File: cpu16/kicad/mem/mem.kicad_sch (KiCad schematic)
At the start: 16 parts, among them J2 BACKPLANE_2x32, U116 74HC688, U117 74HC688, U118 62256, U119 62256, U120 74HC574, U142 74HC32, U161 74HC04

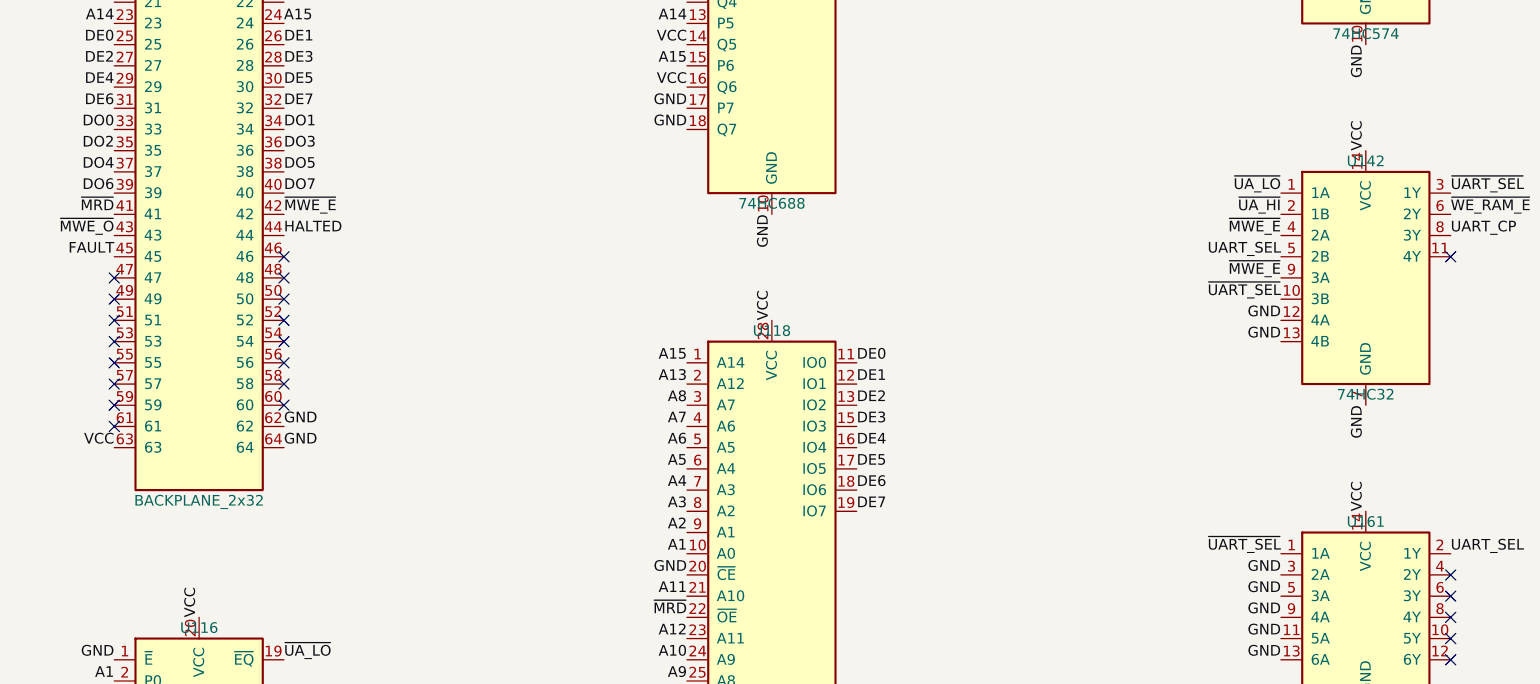
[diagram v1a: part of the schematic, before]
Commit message: Anakart: bekleme durumlu saat kartı, bellek ve önbellek kartları (kapı seviyesi)
Saat kartı: ~WAIT (10 kΩ ile 1'e çekili) s7'nin ortasında W flip-flop'una örneklenir;
W = 1 iken CLK ve WR_WIN kapalı kalır, her bekleme tam bir CPU saati (8 OSC) sürer.
TCLK (uzatılmayan OSC/8, Johnson Q1) ve tamponlu OSC arka panele çıkar. ADIM kipinde
bir basış bekleme turları dahil tam bir döngü. 9 → 10 entegre.

Bellek kartı (bellek, 31 entegre): ~IO çözümü, 4 × 74HC273 bank register'ı (reset
0/32/33/34, geri okuma), PA14..PA19, Flash SST39SF010A + RAM AS6C4008 8 bit, TCLK ile
yürüyen bayt sıralayıcı, boş bölge 0xFF, DE/DO çekme dirençleri.

Önbellek kartı (onbellek, 37 entegre): 2 KB doğrudan eşlemeli, 1024 kelimelik satır,
etiket [19:11] + geçerli, 74HC688 karşılaştırma, write-through, yazma gözetleme (RAM:
güncelle, Flash: geçersiz kıl), reset'te sayıcıyla etiket temizleme, CACHE_CTRL, 4 ×
74HC590 isabet/ıskalama sayacı; ana belleğe giden her erişime tam MEM_WAIT = 2 bekleme.

machine-board.ts: buildMachineBoard({ cards }) ve GateMachine (CPU + saat + bellek +
önbellek; ek kartlar için kanca). bus-master.ts: CPU kartı yerine arka paneli süren
düzenek (Machine'in veri yolu izini kartlarda yeniden oynatmak için).

KiCad: bellek (A2) ve onbellek (A1) projeleri, kart klasöründe BOM; arka panel netleri
BACKPLANE'den. npm run cpu16 -- board artık anakartın özetini ve ERC'sini de yazar.

Testler: anakart-bellek.test.ts (BIOS açılışı, monitör komutları, F ile Flash yükleme,
64 bank/gözetleme/sayaç senaryosu, 1 MB harita — her erişimde değer, bekleme, bank,
sayaç), anakart-sistem.test.ts (saat kartı bekleme turları ve ADIM kipi; CPU dahil
tam sistem Machine ile komut komut: RAM'den programlar, sınama programı, BIOS açılışı).

Co-Authored-By: Claude Opus 5.5 (1M context) <noreply@anthropic.com>
Claude-Session: https://claude.ai/code/session_018J8WVuECVRbQJyCbmF6Nsi
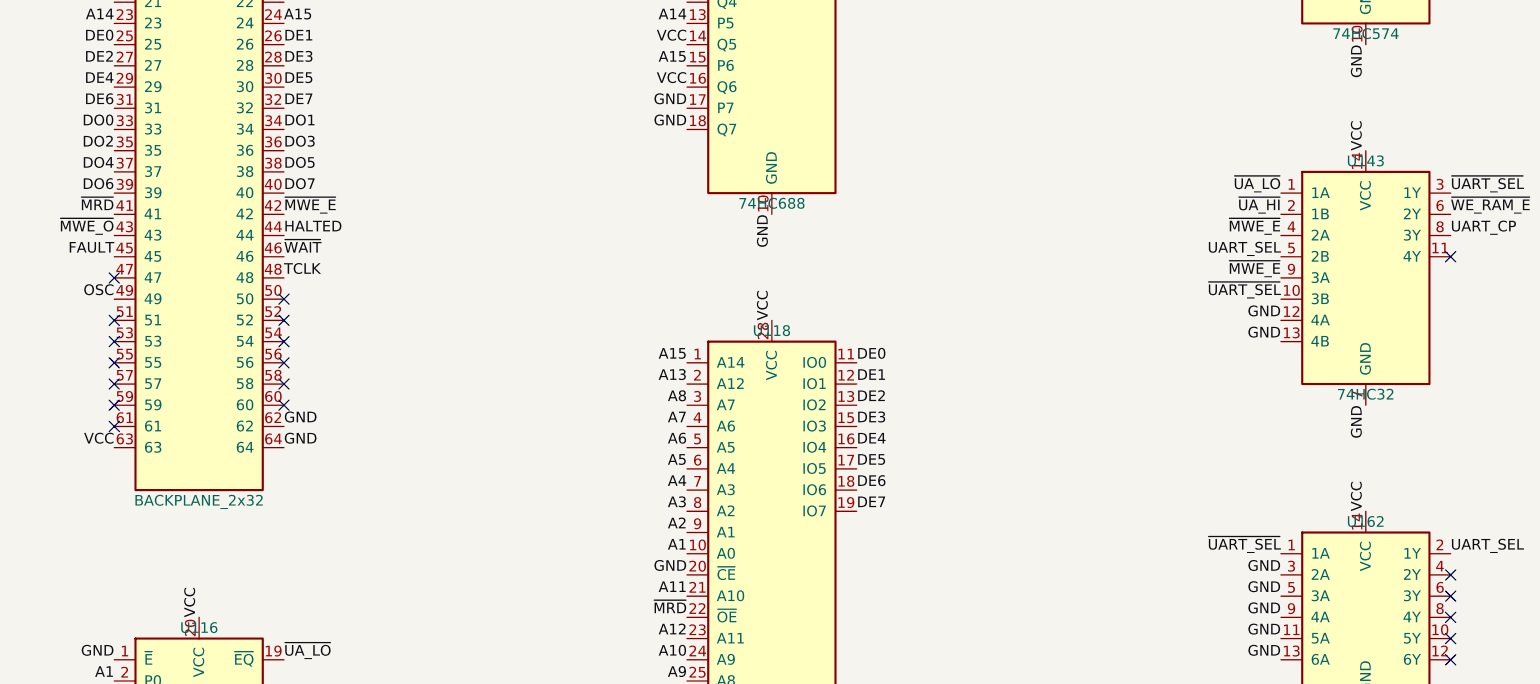
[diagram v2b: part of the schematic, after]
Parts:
- C157: Gorev U142 dekuplaj -> U143 dekuplaj
- C158: Gorev U161 dekuplaj -> U162 dekuplaj
- renumbered U142 to U143, U161 to U162
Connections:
- net ~{WAIT}: now reaches J2.46
- net TCLK: now reaches J2.48
- net OSC: now reaches J2.49
- no-connect marks 30 -> 27
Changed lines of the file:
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@@
   (symbol (lib_id "cpu16:74HC32") (at 195.58 111.76 0) (unit 1)
     (in_bom yes) (on_board yes) (dnp no)
-    (property "Reference" "U142" (at 195.58 97.79 0) (effects (font (size 1.27 1.27))))
+    (property "Reference" "U143" (at 195.58 97.79 0) (effects (font (size 1.27 1.27))))
     (property "Value" "74HC32" (at 195.58 125.73 0) (effects (font (size 1.27 1.27))))
     (property "Footprint" "Package_DIP:DIP-14_W7.62mm" (at 195.58 111.76 0) (effects (font (size 1.27 1.27)) hide))
@@
     (pin "13")
     (pin "14")
-    (instances (project "mem" (path "/2ef92f41-0000-4000-8000-000000000001" (reference "U142") (unit 1))))
+    (instances (project "mem" (path "/2ef92f41-0000-4000-8000-000000000001" (reference "U143") (unit 1))))
   )
   (symbol (lib_id "cpu16:74HC04") (at 195.58 152.4 0) (unit 1)
     (in_bom yes) (on_board yes) (dnp no)
-    (property "Reference" "U161" (at 195.58 140.97 0) (effects (font (size 1.27 1.27))))
+    (property "Reference" "U162" (at 195.58 140.97 0) (effects (font (size 1.27 1.27))))
     (property "Value" "74HC04" (at 195.58 163.83 0) (effects (font (size 1.27 1.27))))
     (property "Footprint" "Package_DIP:DIP-14_W7.62mm" (at 195.58 152.4 0) (effects (font (size 1.27 1.27)) hide))
@@
     (pin "13")
     (pin "14")
-    (instances (project "mem" (path "/2ef92f41-0000-4000-8000-000000000001" (reference "U161") (unit 1))))
+    (instances (project "mem" (path "/2ef92f41-0000-4000-8000-000000000001" (reference "U162") (unit 1))))
   )
   (symbol (lib_id "cpu16:C_100U") (at 195.58 182.88 0) (unit 1)
@@
     (property "Footprint" "Capacitor_THT:C_Disc_D5.0mm_W2.5mm_P5.00mm" (at 266.7 99.06 0) (effects (font (size 1.27 1.27)) hide))
     (property "Datasheet" "" (at 266.7 99.06 0) (effects (font (size 1.27 1.27)) hide))
-    (property "Gorev" "U142 dekuplaj" (at 266.7 99.06 0) (effects (font (size 1.27 1.27)) hide))
+    (property "Gorev" "U143 dekuplaj" (at 266.7 99.06 0) (effects (font (size 1.27 1.27)) hide))
     (pin "1")
     (pin "2")
@@
     (property "Footprint" "Capacitor_THT:C_Disc_D5.0mm_W2.5mm_P5.00mm" (at 266.7 121.92 0) (effects (font (size 1.27 1.27)) hide))
     (property "Datasheet" "" (at 266.7 121.92 0) (effects (font (size 1.27 1.27)) hide))
-    (property "Gorev" "U161 dekuplaj" (at 266.7 121.92 0) (effects (font (size 1.27 1.27)) hide))
+    (property "Gorev" "U162 dekuplaj" (at 266.7 121.92 0) (effects (font (size 1.27 1.27)) hide))
     (pin "1")
     (pin "2")
@@
   (label "FAULT" (at 45.72 109.22 180) (fields_autoplaced) (effects (font (size 1.27 1.27)) (justify right bottom)))
   (no_connect (at 45.72 111.76))
-  (no_connect (at 45.72 114.3))
+  (label "OSC" (at 45.72 114.3 180) (fields_autoplaced) (effects (font (size 1.27 1.27)) (justify right bottom)))
   (no_connect (at 45.72 116.84))
   (no_connect (at 45.72 119.38))
@@
   (label "~{MWE_E}" (at 66.04 104.14 0) (fields_autoplaced) (effects (font (size 1.27 1.27)) (justify left bottom)))
   (label "HALTED" (at 66.04 106.68 0) (fields_autoplaced) (effects (font (size 1.27 1.27)) (justify left bottom)))
-  (no_connect (at 66.04 109.22))
-  (no_connect (at 66.04 111.76))
+  (label "~{WAIT}" (at 66.04 109.22 0) (fields_autoplaced) (effects (font (size 1.27 1.27)) (justify left bottom)))
+  (label "TCLK" (at 66.04 111.76 0) (fields_autoplaced) (effects (font (size 1.27 1.27)) (justify left bottom)))
   (no_connect (at 66.04 114.3))
   (no_connect (at 66.04 116.84))
